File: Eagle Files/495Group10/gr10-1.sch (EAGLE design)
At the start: 51 parts, among them Y1 16MHz, Y2 16 MHZ

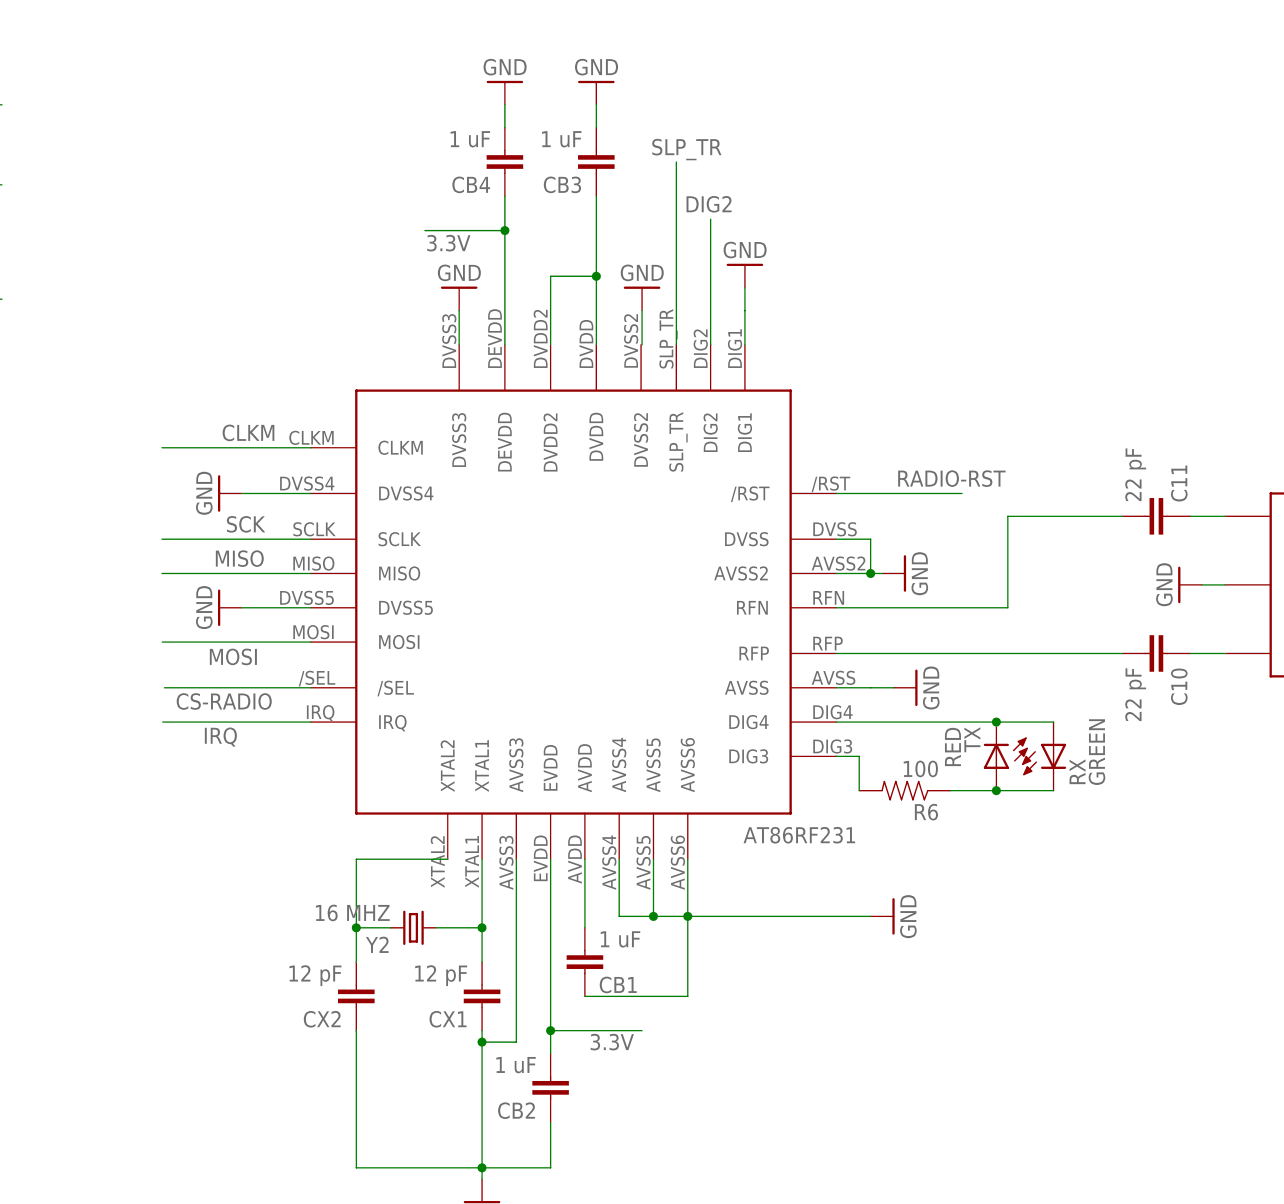
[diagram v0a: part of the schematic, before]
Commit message: Fixed a few things in the Main Board.
I updated the main board to use the new Radio part.
I also changed the ground plane distance to 20 mil.

--Arthur

git-svn-id: http://cd-net.net/CPE496/trunk@86 05b6d0e0-c345-4a8e-a5b7-579c8bd0b646
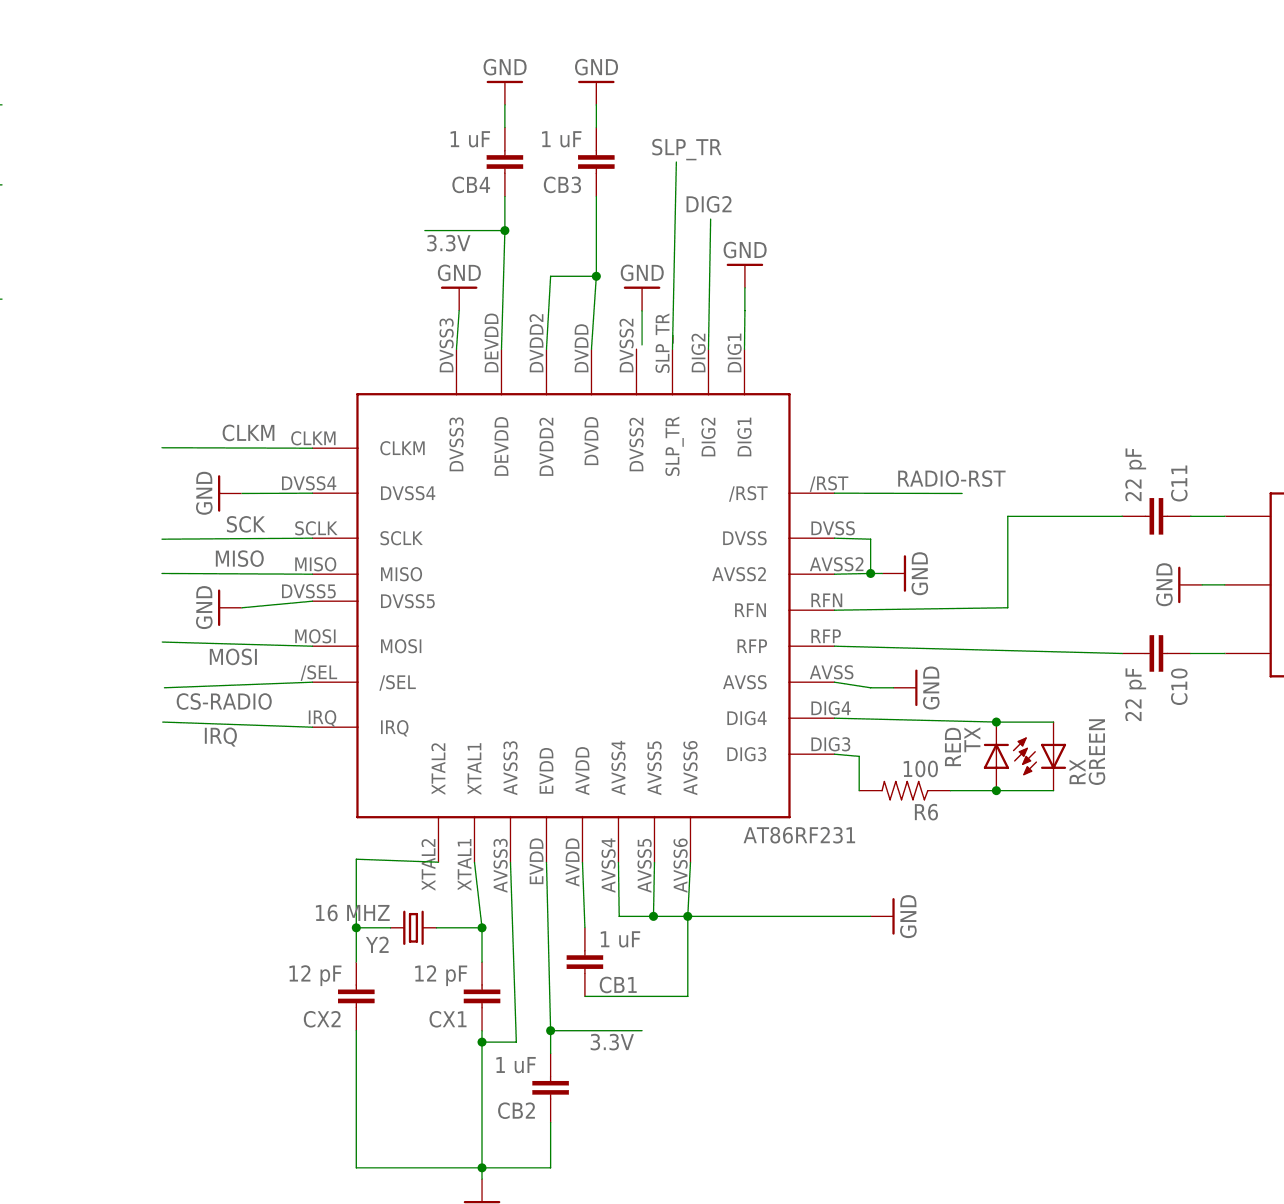
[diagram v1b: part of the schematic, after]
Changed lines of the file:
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@@
 <pinref part="U$3" gate="G$1" pin="DIG1"/>
 <pinref part="GND23" gate="1" pin="GND"/>
-<wire x1="161.29" y1="76.2" x2="161.29" y2="80.01" width="0.1524" layer="91"/>
+<wire x1="161.24" y1="75.72" x2="161.29" y2="80.01" width="0.1524" layer="91"/>
 <wire x1="161.29" y1="80.01" x2="161.29" y2="82.55" width="0.1524" layer="91"/>
 </segment>
@@
 <pinref part="U$3" gate="G$1" pin="AVSS2"/>
 <pinref part="GND24" gate="1" pin="GND"/>
-<wire x1="171.45" y1="50.8" x2="175.26" y2="50.8" width="0.1524" layer="91"/>
+<wire x1="171.24" y1="50.72" x2="175.26" y2="50.8" width="0.1524" layer="91"/>
 <pinref part="U$3" gate="G$1" pin="DVSS"/>
 <wire x1="175.26" y1="50.8" x2="176.53" y2="50.8" width="0.1524" layer="91"/>
-<wire x1="171.45" y1="54.61" x2="175.26" y2="54.61" width="0.1524" layer="91"/>
+<wire x1="171.24" y1="54.72" x2="175.26" y2="54.61" width="0.1524" layer="91"/>
 <wire x1="175.26" y1="54.61" x2="175.26" y2="50.8" width="0.1524" layer="91"/>
 <junction x="175.26" y="50.8"/>
@@
 <segment>
 <pinref part="U$3" gate="G$1" pin="AVSS"/>
-<wire x1="171.45" y1="38.1" x2="175.26" y2="38.1" width="0.1524" layer="91"/>
+<wire x1="171.24" y1="38.72" x2="175.26" y2="38.1" width="0.1524" layer="91"/>
 <pinref part="GND29" gate="1" pin="GND"/>
 <wire x1="177.8" y1="38.1" x2="175.26" y2="38.1" width="0.1524" layer="91"/>
@@
 <pinref part="GND25" gate="1" pin="GND"/>
 <pinref part="U$3" gate="G$1" pin="AVSS4"/>
-<wire x1="147.32" y1="19.05" x2="147.32" y2="12.7" width="0.1524" layer="91"/>
+<wire x1="147.24" y1="18.72" x2="147.32" y2="12.7" width="0.1524" layer="91"/>
 <wire x1="147.32" y1="12.7" x2="151.13" y2="12.7" width="0.1524" layer="91"/>
 <pinref part="U$3" gate="G$1" pin="AVSS5"/>
 <wire x1="151.13" y1="12.7" x2="154.94" y2="12.7" width="0.1524" layer="91"/>
 <wire x1="154.94" y1="12.7" x2="175.26" y2="12.7" width="0.1524" layer="91"/>
-<wire x1="151.13" y1="19.05" x2="151.13" y2="12.7" width="0.1524" layer="91"/>
+<wire x1="151.24" y1="18.72" x2="151.13" y2="12.7" width="0.1524" layer="91"/>
 <junction x="151.13" y="12.7"/>
 <pinref part="U$3" gate="G$1" pin="AVSS6"/>
-<wire x1="154.94" y1="19.05" x2="154.94" y2="12.7" width="0.1524" layer="91"/>
+<wire x1="155.24" y1="18.72" x2="154.94" y2="12.7" width="0.1524" layer="91"/>
 <junction x="154.94" y="12.7"/>
 <pinref part="CB1" gate="G$1" pin="1"/>
@@
 <wire x1="139.7" y1="-15.24" x2="132.08" y2="-15.24" width="0.1524" layer="91"/>
 <pinref part="U$3" gate="G$1" pin="AVSS3"/>
-<wire x1="135.89" y1="19.05" x2="135.89" y2="-1.27" width="0.1524" layer="91"/>
+<wire x1="135.24" y1="18.72" x2="135.89" y2="-1.27" width="0.1524" layer="91"/>
 <wire x1="135.89" y1="-1.27" x2="132.08" y2="-1.27" width="0.1524" layer="91"/>
 <junction x="132.08" y="-1.27"/>
@@
 <pinref part="U$3" gate="G$1" pin="DVSS3"/>
 <pinref part="GND21" gate="1" pin="GND"/>
-<wire x1="129.54" y1="76.2" x2="129.54" y2="80.01" width="0.1524" layer="91"/>
+<wire x1="129.24" y1="75.72" x2="129.54" y2="80.01" width="0.1524" layer="91"/>
 </segment>
 <segment>
 <pinref part="GND28" gate="1" pin="GND"/>
 <pinref part="U$3" gate="G$1" pin="DVSS4"/>
-<wire x1="105.41" y1="59.69" x2="113.03" y2="59.69" width="0.1524" layer="91"/>
+<wire x1="105.41" y1="59.69" x2="113.24" y2="59.72" width="0.1524" layer="91"/>
 </segment>
 <segment>
 <pinref part="GND27" gate="1" pin="GND"/>
 <pinref part="U$3" gate="G$1" pin="DVSS5"/>
-<wire x1="105.41" y1="46.99" x2="113.03" y2="46.99" width="0.1524" layer="91"/>
+<wire x1="105.41" y1="46.99" x2="113.24" y2="47.72" width="0.1524" layer="91"/>
 </segment>
 <segment>
@@
 <segment>
 <pinref part="U$3" gate="G$1" pin="MOSI"/>
-<wire x1="113.03" y1="43.18" x2="96.55" y2="43.18" width="0.1524" layer="91"/>
+<wire x1="113.24" y1="42.72" x2="96.55" y2="43.18" width="0.1524" layer="91"/>
 <label x="107.28" y="42.42" size="1.778" layer="95" rot="R180"/>
 </segment>
@@
 <pinref part="U$3" gate="G$1" pin="DEVDD"/>
 <pinref part="CB4" gate="G$1" pin="1"/>
-<wire x1="134.62" y1="76.2" x2="134.62" y2="88.9" width="0.1524" layer="91"/>
+<wire x1="134.24" y1="75.72" x2="134.62" y2="88.9" width="0.1524" layer="91"/>
 <wire x1="134.62" y1="88.9" x2="134.62" y2="92.71" width="0.1524" layer="91"/>
 <wire x1="134.62" y1="88.9" x2="125.73" y2="88.9" width="0.1524" layer="91"/>
@@
 <pinref part="U$3" gate="G$1" pin="EVDD"/>
 <pinref part="CB2" gate="G$1" pin="2"/>
-<wire x1="139.7" y1="19.05" x2="139.7" y2="0" width="0.1524" layer="91"/>
+<wire x1="139.24" y1="18.72" x2="139.7" y2="0" width="0.1524" layer="91"/>
 <wire x1="139.7" y1="0" x2="139.7" y2="-2.54" width="0.1524" layer="91"/>
 <wire x1="139.7" y1="0" x2="149.86" y2="0" width="0.1524" layer="91"/>
@@
 <segment>
 <pinref part="U$3" gate="G$1" pin="SCLK"/>
-<wire x1="113.03" y1="54.61" x2="96.52" y2="54.61" width="0.1524" layer="91"/>
+<wire x1="113.24" y1="54.72" x2="96.52" y2="54.61" width="0.1524" layer="91"/>
 <label x="107.95" y="57.15" size="1.778" layer="95" rot="R180"/>
 </segment>
@@
 <segment>
 <pinref part="U$3" gate="G$1" pin="MISO"/>
-<wire x1="113.03" y1="50.8" x2="96.52" y2="50.8" width="0.1524" layer="91"/>
+<wire x1="113.24" y1="50.72" x2="96.52" y2="50.8" width="0.1524" layer="91"/>
 <label x="107.95" y="53.34" size="1.778" layer="95" rot="R180"/>
 </segment>
@@
 <segment>
 <pinref part="U$3" gate="G$1" pin="/SEL"/>
-<wire x1="113.03" y1="38.1" x2="96.79" y2="38.1" width="0.1524" layer="91"/>
+<wire x1="113.24" y1="38.72" x2="96.79" y2="38.1" width="0.1524" layer="91"/>
 <label x="108.839" y="37.465" size="1.778" layer="95" rot="R180"/>
 </segment>
@@
 <segment>
 <pinref part="U$3" gate="G$1" pin="/RST"/>
-<wire x1="171.45" y1="59.69" x2="185.42" y2="59.69" width="0.1524" layer="91"/>
+<wire x1="171.24" y1="59.72" x2="185.42" y2="59.69" width="0.1524" layer="91"/>
 <label x="190.246" y="62.23" size="1.778" layer="95" rot="R180"/>
 </segment>
@@
 <segment>
 <pinref part="U$3" gate="G$1" pin="SLP_TR"/>
-<wire x1="153.67" y1="76.2" x2="153.67" y2="96.52" width="0.1524" layer="91"/>
+<wire x1="153.24" y1="75.72" x2="153.67" y2="96.52" width="0.1524" layer="91"/>
 <label x="158.75" y="99.06" size="1.778" layer="95" rot="R180"/>
 </segment>
@@
 <segment>
 <pinref part="U$3" gate="G$1" pin="IRQ"/>
-<wire x1="113.03" y1="34.29" x2="96.6" y2="34.29" width="0.1524" layer="91"/>
+<wire x1="113.24" y1="33.72" x2="96.6" y2="34.29" width="0.1524" layer="91"/>
 <label x="104.966" y="33.655" size="1.778" layer="95" rot="R180"/>
 </segment>
@@
 <segment>
 <pinref part="U$3" gate="G$1" pin="DIG2"/>
-<wire x1="157.48" y1="76.2" x2="157.48" y2="90.17" width="0.1524" layer="91"/>
+<wire x1="157.24" y1="75.72" x2="157.48" y2="90.17" width="0.1524" layer="91"/>
 <label x="160.02" y="92.71" size="1.778" layer="95" rot="R180"/>
 </segment>
@@
 <segment>
 <pinref part="U$3" gate="G$1" pin="DVDD"/>
-<wire x1="144.78" y1="76.2" x2="144.78" y2="83.82" width="0.1524" layer="91"/>
+<wire x1="144.24" y1="75.72" x2="144.78" y2="83.82" width="0.1524" layer="91"/>
 <pinref part="U$3" gate="G$1" pin="DVDD2"/>
-<wire x1="139.7" y1="76.2" x2="139.7" y2="83.82" width="0.1524" layer="91"/>
+<wire x1="139.24" y1="75.72" x2="139.7" y2="83.82" width="0.1524" layer="91"/>
 <wire x1="139.7" y1="83.82" x2="144.78" y2="83.82" width="0.1524" layer="91"/>
 <pinref part="CB3" gate="G$1" pin="1"/>
@@
 <pinref part="U$3" gate="G$1" pin="AVDD"/>
 <pinref part="CB1" gate="G$1" pin="2"/>
-<wire x1="143.51" y1="19.05" x2="143.51" y2="11.43" width="0.1524" layer="91"/>
+<wire x1="143.24" y1="18.72" x2="143.51" y2="11.43" width="0.1524" layer="91"/>
 </segment>
 </net>
@@
 <pinref part="U$3" gate="G$1" pin="XTAL1"/>
 <pinref part="CX1" gate="G$1" pin="2"/>
-<wire x1="132.08" y1="19.05" x2="132.08" y2="11.43" width="0.1524" layer="91"/>
+<wire x1="131.24" y1="18.72" x2="132.08" y2="11.43" width="0.1524" layer="91"/>
 <pinref part="Y2" gate="G$1" pin="1"/>
 <wire x1="132.08" y1="11.43" x2="132.08" y2="7.62" width="0.1524" layer="91"/>
@@
 <pinref part="U$3" gate="G$1" pin="XTAL2"/>
 <pinref part="CX2" gate="G$1" pin="2"/>
-<wire x1="128.27" y1="19.05" x2="118.11" y2="19.05" width="0.1524" layer="91"/>
+<wire x1="127.24" y1="18.72" x2="118.11" y2="19.05" width="0.1524" layer="91"/>
 <wire x1="118.11" y1="19.05" x2="118.11" y2="11.43" width="0.1524" layer="91"/>
 <pinref part="Y2" gate="G$1" pin="2"/>
@@
 <pinref part="U$3" gate="G$1" pin="DIG4"/>
 <pinref part="TX" gate="G$1" pin="C"/>
-<wire x1="171.45" y1="34.29" x2="189.23" y2="34.29" width="0.1524" layer="91"/>
+<wire x1="171.24" y1="34.72" x2="189.23" y2="34.29" width="0.1524" layer="91"/>
 <pinref part="RX" gate="G$1" pin="A"/>
 <wire x1="189.23" y1="34.29" x2="195.58" y2="34.29" width="0.1524" layer="91"/>
@@
 <pinref part="R6" gate="G$1" pin="2"/>
 <pinref part="U$3" gate="G$1" pin="DIG3"/>
-<wire x1="171.45" y1="30.48" x2="173.99" y2="30.48" width="0.1524" layer="91"/>
+<wire x1="171.24" y1="30.72" x2="173.99" y2="30.48" width="0.1524" layer="91"/>
 </segment>
 </net>
@@
 <segment>
 <pinref part="U$3" gate="G$1" pin="RFN"/>
-<wire x1="171.45" y1="46.99" x2="190.5" y2="46.99" width="0.1524" layer="91"/>
+<wire x1="171.24" y1="46.72" x2="190.5" y2="46.99" width="0.1524" layer="91"/>
 <pinref part="C11" gate="G$1" pin="2"/>
 <wire x1="190.5" y1="46.99" x2="190.5" y2="57.15" width="0.1524" layer="91"/>
@@
 <pinref part="U$3" gate="G$1" pin="RFP"/>
 <pinref part="C10" gate="G$1" pin="2"/>
-<wire x1="171.45" y1="41.91" x2="203.2" y2="41.91" width="0.1524" layer="91"/>
+<wire x1="171.24" y1="42.72" x2="203.2" y2="41.91" width="0.1524" layer="91"/>
 </segment>
 </net>
@@
 <segment>
 <pinref part="U$3" gate="G$1" pin="CLKM"/>
-<wire x1="113.03" y1="64.77" x2="96.52" y2="64.77" width="0.1524" layer="91"/>
+<wire x1="113.24" y1="64.72" x2="96.52" y2="64.77" width="0.1524" layer="91"/>
 <label x="109.22" y="67.31" size="1.778" layer="95" rot="R180"/>
 </segment>
